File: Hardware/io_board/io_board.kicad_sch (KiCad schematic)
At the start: 32 parts, among them J1 Conn_01x40, J2 Conn_02x06_Odd_Even, J3 Mini-DIN-6, J4 Conn_02x10_Odd_Even, J5 Conn_01x04_Male, U2 W65C22NxP, U3 74LS14, U4 74HC137

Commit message: update for kicad 6
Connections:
- net GND: now also J4.13 (Pin_13)
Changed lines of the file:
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@@
   (junction (at 181.61 138.43) (diameter 0) (color 0 0 0 0)
   )
+  (junction (at 82.55 85.09) (diameter 0) (color 0 0 0 0)
+  )
   (junction (at 240.03 119.38) (diameter 0) (color 0 0 0 0)
   )
+  (junction (at 48.26 83.82) (diameter 0) (color 0 0 0 0)
+  )
   (junction (at 163.83 22.86) (diameter 0) (color 0 0 0 0)
   )
@@
     (stroke (width 0) (type default) (color 0 0 0 0))
   )
+  (wire (pts (xy 161.29 146.05) (xy 168.91 146.05))
+    (stroke (width 0) (type default) (color 0 0 0 0))
+  )
   (wire (pts (xy 181.61 153.67) (xy 186.69 153.67))
     (stroke (width 0) (type default) (color 0 0 0 0))
@@
     (stroke (width 0) (type default) (color 0 0 0 0))
   )
-  (wire (pts (xy 71.12 85.09) (xy 85.09 85.09))
+  (wire (pts (xy 71.12 85.09) (xy 82.55 85.09))
     (stroke (width 0) (type default) (color 0 0 0 0))
   )
@@
     (stroke (width 0) (type default) (color 0 0 0 0))
   )
+  (wire (pts (xy 48.26 83.82) (xy 46.99 83.82))
+    (stroke (width 0) (type default) (color 0 0 0 0))
+  )
   (wire (pts (xy 180.34 90.17) (xy 180.34 88.9))
     (stroke (width 0) (type default) (color 0 0 0 0))
@@
     (stroke (width 0) (type default) (color 0 0 0 0))
   )
-  (wire (pts (xy 53.34 83.82) (xy 46.99 83.82))
+  (wire (pts (xy 53.34 83.82) (xy 48.26 83.82))
     (stroke (width 0) (type default) (color 0 0 0 0))
   )
@@
   )
   (wire (pts (xy 101.6 83.82) (xy 96.52 83.82))
+    (stroke (width 0) (type default) (color 0 0 0 0))
+  )
+  (wire (pts (xy 82.55 85.09) (xy 85.09 85.09))
     (stroke (width 0) (type default) (color 0 0 0 0))
   )
@@
     (pin "1")
     (pin "2")
+    (pin "3")
+    (pin "4")
+    (pin "5")
+    (pin "6")
+    (pin "8")
+    (pin "9")
+    (pin "10")
+    (pin "11")
+    (pin "12")
+    (pin "13")
+    (pin "14")
+    (pin "7")
   )
   (symbol (lib_id "74xx:74LS14") (at 189.23 99.06 180) (unit 2)
@@
       (effects (font (size 1.27 1.27)) hide)
     )
+    (pin "1")
+    (pin "2")
     (pin "3")
     (pin "4")
+    (pin "5")
+    (pin "6")
+    (pin "8")
+    (pin "9")
+    (pin "10")
+    (pin "11")
+    (pin "12")
+    (pin "13")
+    (pin "14")
+    (pin "7")
   )
   (symbol (lib_id "74xx:74LS14") (at 48.26 161.29 0) (unit 3)
@@
       (effects (font (size 1.27 1.27)) hide)
     )
+    (pin "1")
+    (pin "2")
+    (pin "3")
+    (pin "4")
     (pin "5")
     (pin "6")
+    (pin "8")
+    (pin "9")
+    (pin "10")
+    (pin "11")
+    (pin "12")
+    (pin "13")
+    (pin "14")
+    (pin "7")
   )
   (symbol (lib_id "74xx:74LS14") (at 48.26 172.72 0) (unit 4)
@@
       (effects (font (size 1.27 1.27)) hide)
     )
+    (pin "1")
+    (pin "2")
+    (pin "3")
+    (pin "4")
+    (pin "5")
+    (pin "6")
     (pin "8")
     (pin "9")
+    (pin "10")
+    (pin "11")
+    (pin "12")
+    (pin "13")
+    (pin "14")
+    (pin "7")
   )
   (symbol (lib_id "74xx:74LS14") (at 196.85 86.36 180) (unit 5)
@@
       (effects (font (size 1.27 1.27)) hide)
     )
+    (pin "1")
+    (pin "2")
+    (pin "3")
+    (pin "4")
+    (pin "5")
+    (pin "6")
+    (pin "8")
+    (pin "9")
     (pin "10")
     (pin "11")
+    (pin "12")
+    (pin "13")
+    (pin "14")
+    (pin "7")
   )
   (symbol (lib_id "74xx:74LS14") (at 213.36 88.9 180) (unit 6)
@@
       (effects (font (size 1.27 1.27)) hide)
     )
+    (pin "1")
+    (pin "2")
+    (pin "3")
+    (pin "4")
+    (pin "5")
+    (pin "6")
+    (pin "8")
+    (pin "9")
+    (pin "10")
+    (pin "11")
     (pin "12")
     (pin "13")
+    (pin "14")
+    (pin "7")
   )
   (symbol (lib_id "74xx:74LS14") (at 240.03 140.97 0) (unit 7)
@@
       (effects (font (size 1.27 1.27)) hide)
     )
+    (pin "1")
+    (pin "2")
+    (pin "3")
+    (pin "4")
+    (pin "5")
+    (pin "6")
+    (pin "8")
+    (pin "9")
+    (pin "10")
+    (pin "11")
+    (pin "12")
+    (pin "13")
     (pin "14")
     (pin "7")
@@
     (pin "1")
   )
+  (symbol (lib_id "power:GND") (at 161.29 146.05 0) (unit 1)
+    (in_bom yes) (on_board yes)
+    (property "Reference" "#PWR0139" (id 0) (at 161.29 152.4 0)
+      (effects (font (size 1.27 1.27)) hide)
+    )
+    (property "Value" "GND" (id 1) (at 161.417 150.4442 0))
+    (property "Footprint" "" (id 2) (at 161.29 146.05 0)
+      (effects (font (size 1.27 1.27)) hide)
+    )
+    (property "Datasheet" "" (id 3) (at 161.29 146.05 0)
+      (effects (font (size 1.27 1.27)) hide)
+    )
+    (pin "1")
+  )
   (symbol (lib_id "74xx:74HC137") (at 119.38 142.24 0) (unit 1)
     (in_bom yes) (on_board yes) (fields_autoplaced)
@@
     (pin "9")
   )
+  (symbol (lib_id "power:PWR_FLAG") (at 48.26 83.82 0) (unit 1)
+    (in_bom yes) (on_board yes) (fields_autoplaced)
+    (property "Reference" "#FLG0101" (id 0) (at 48.26 81.915 0)
+      (effects (font (size 1.27 1.27)) hide)
+    )
+    (property "Value" "PWR_FLAG" (id 1) (at 48.26 80.2442 0))
+    (property "Footprint" "" (id 2) (at 48.26 83.82 0)
+      (effects (font (size 1.27 1.27)) hide)
+    )
+    (property "Datasheet" "~" (id 3) (at 48.26 83.82 0)
+      (effects (font (size 1.27 1.27)) hide)
+    )
+    (pin "1")
+  )
+  (symbol (lib_id "power:PWR_FLAG") (at 82.55 85.09 0) (unit 1)
+    (in_bom yes) (on_board yes) (fields_autoplaced)
+    (property "Reference" "#FLG0102" (id 0) (at 82.55 83.185 0)
+      (effects (font (size 1.27 1.27)) hide)
+    )
+    (property "Value" "PWR_FLAG" (id 1) (at 82.55 81.5142 0))
+    (property "Footprint" "" (id 2) (at 82.55 85.09 0)
+      (effects (font (size 1.27 1.27)) hide)
+    )
+    (property "Datasheet" "~" (id 3) (at 82.55 85.09 0)
+      (effects (font (size 1.27 1.27)) hide)
+    )
+    (pin "1")
+  )
   (sheet_instances
     (path "/" (page "1"))
   )
   (symbol_instances
+    (path "/af339d33-3531-42fd-aaba-73cbd73b724b"
+      (reference "#FLG0101") (unit 1) (value "PWR_FLAG") (footprint "")
+    )
+    (path "/e0ece25e-4db1-472a-896f-76e59008368f"
+      (reference "#FLG0102") (unit 1) (value "PWR_FLAG") (footprint "")
+    )
     (path "/00000000-0000-0000-0000-00005fd64472"
       (reference "#PWR0101") (unit 1) (value "+5V") (footprint "")
@@
       (reference "#PWR0138") (unit 1) (value "+5V") (footprint "")
     )
+    (path "/7512532e-08f1-4a9c-83bd-4429d275ecbb"
+      (reference "#PWR0139") (unit 1) (value "GND") (footprint "")
+    )
     (path "/00000000-0000-0000-0000-00005febb5d8"

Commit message: update io board
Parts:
- D1, D2, D3, D4, D5, D6, D7, D8: footprint LED_THT:LED_D3.0mm_Horizontal_O3.81mm_Z6.0mm -> w_conn_av:LED_D3.0mm_Horizontal_O3.81mm_Z6.0mm_2
- J3: footprint mini-din:MINI-DIN-6-FULL-SHIELD -> Custom_Footprints:Connector_Mini-DIN_Female_6Pin_2rows
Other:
- company: (none) -> Six Pixels
- title: (none) -> IO Board
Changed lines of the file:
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@@
 (kicad_sch (version 20211123) (generator eeschema)
   (paper "A4")
+  (title_block
+    (title "IO Board")
+    (date "2023-02-11")
+    (rev "${VERSION}")
+    (company "Six Pixels")
+    (comment 1 "Added pin header for PS/2")
+  )
   (junction (at 203.2 118.11) (diameter 0) (color 0 0 0 0)
   )
@@
     (property "Reference" "J3" (id 0) (at 215.9 108.7882 0))
     (property "Value" "Mini-DIN-6" (id 1) (at 217.17 110.49 0))
-    (property "Footprint" "mini-din:MINI-DIN-6-FULL-SHIELD" (id 2) (at 215.9 118.11 0)
+    (property "Footprint" "Custom_Footprints:Connector_Mini-DIN_Female_6Pin_2rows" (id 2) (at 215.9 118.11 0)
       (effects (font (size 1.27 1.27)) hide)
     )
@@
     (property "Reference" "D1" (id 0) (at 105.5878 40.2082 0))
     (property "Value" "LED" (id 1) (at 105.5878 42.5196 0))
-    (property "Footprint" "LED_THT:LED_D3.0mm_Horizontal_O3.81mm_Z6.0mm" (id 2) (at 105.41 45.72 0)
+    (property "Footprint" "w_conn_av:LED_D3.0mm_Horizontal_O3.81mm_Z6.0mm_2" (id 2) (at 105.41 45.72 0)
       (effects (font (size 1.27 1.27)) hide)
     )
@@
     (property "Reference" "D2" (id 0) (at 105.5878 46.5582 0))
     (property "Value" "LED" (id 1) (at 105.5878 48.8696 0))
-    (property "Footprint" "LED_THT:LED_D3.0mm_Horizontal_O3.81mm_Z6.0mm" (id 2) (at 105.41 52.07 0)
+    (property "Footprint" "w_conn_av:LED_D3.0mm_Horizontal_O3.81mm_Z6.0mm_2" (id 2) (at 105.41 52.07 0)
       (effects (font (size 1.27 1.27)) hide)
     )
@@
     (property "Reference" "D3" (id 0) (at 105.5878 52.9082 0))
     (property "Value" "LED" (id 1) (at 105.5878 55.2196 0))
-    (property "Footprint" "LED_THT:LED_D3.0mm_Horizontal_O3.81mm_Z6.0mm" (id 2) (at 105.41 58.42 0)
+    (property "Footprint" "w_conn_av:LED_D3.0mm_Horizontal_O3.81mm_Z6.0mm_2" (id 2) (at 105.41 58.42 0)
       (effects (font (size 1.27 1.27)) hide)
     )
@@
     (property "Reference" "D4" (id 0) (at 105.5878 59.2582 0))
     (property "Value" "LED" (id 1) (at 105.5878 61.5696 0))
-    (property "Footprint" "LED_THT:LED_D3.0mm_Horizontal_O3.81mm_Z6.0mm" (id 2) (at 105.41 64.77 0)
+    (property "Footprint" "w_conn_av:LED_D3.0mm_Horizontal_O3.81mm_Z6.0mm_2" (id 2) (at 105.41 64.77 0)
       (effects (font (size 1.27 1.27)) hide)
     )
@@
     (property "Reference" "D5" (id 0) (at 105.5878 65.6082 0))
     (property "Value" "LED" (id 1) (at 105.5878 67.9196 0))
-    (property "Footprint" "LED_THT:LED_D3.0mm_Horizontal_O3.81mm_Z6.0mm" (id 2) (at 105.41 71.12 0)
+    (property "Footprint" "w_conn_av:LED_D3.0mm_Horizontal_O3.81mm_Z6.0mm_2" (id 2) (at 105.41 71.12 0)
       (effects (font (size 1.27 1.27)) hide)
     )
@@
     (property "Reference" "D6" (id 0) (at 105.5878 71.9582 0))
     (property "Value" "LED" (id 1) (at 105.5878 74.2696 0))
-    (property "Footprint" "LED_THT:LED_D3.0mm_Horizontal_O3.81mm_Z6.0mm" (id 2) (at 105.41 77.47 0)
+    (property "Footprint" "w_conn_av:LED_D3.0mm_Horizontal_O3.81mm_Z6.0mm_2" (id 2) (at 105.41 77.47 0)
       (effects (font (size 1.27 1.27)) hide)
     )
@@
     (property "Reference" "D7" (id 0) (at 105.5878 78.3082 0))
     (property "Value" "LED" (id 1) (at 105.5878 80.6196 0))
-    (property "Footprint" "LED_THT:LED_D3.0mm_Horizontal_O3.81mm_Z6.0mm" (id 2) (at 105.41 83.82 0)
+    (property "Footprint" "w_conn_av:LED_D3.0mm_Horizontal_O3.81mm_Z6.0mm_2" (id 2) (at 105.41 83.82 0)
       (effects (font (size 1.27 1.27)) hide)
     )
@@
     (property "Reference" "D8" (id 0) (at 105.5878 84.6582 0))
     (property "Value" "LED" (id 1) (at 105.5878 86.9696 0))
-    (property "Footprint" "LED_THT:LED_D3.0mm_Horizontal_O3.81mm_Z6.0mm" (id 2) (at 105.41 90.17 0)
+    (property "Footprint" "w_conn_av:LED_D3.0mm_Horizontal_O3.81mm_Z6.0mm_2" (id 2) (at 105.41 90.17 0)
       (effects (font (size 1.27 1.27)) hide)
     )
@@
     )
     (path "/00000000-0000-0000-0000-00005ff231e9"
-      (reference "D1") (unit 1) (value "LED") (footprint "LED_THT:LED_D3.0mm_Horizontal_O3.81mm_Z6.0mm")
+      (reference "D1") (unit 1) (value "LED") (footprint "w_conn_av:LED_D3.0mm_Horizontal_O3.81mm_Z6.0mm_2")
     )
     (path "/00000000-0000-0000-0000-00005ff4ddfd"
-      (reference "D2") (unit 1) (value "LED") (footprint "LED_THT:LED_D3.0mm_Horizontal_O3.81mm_Z6.0mm")
+      (reference "D2") (unit 1) (value "LED") (footprint "w_conn_av:LED_D3.0mm_Horizontal_O3.81mm_Z6.0mm_2")
     )
     (path "/00000000-0000-0000-0000-00005ff55550"
-      (reference "D3") (unit 1) (value "LED") (footprint "LED_THT:LED_D3.0mm_Horizontal_O3.81mm_Z6.0mm")
+      (reference "D3") (unit 1) (value "LED") (footprint "w_conn_av:LED_D3.0mm_Horizontal_O3.81mm_Z6.0mm_2")
     )
     (path "/00000000-0000-0000-0000-00005ff5cdd6"
-      (reference "D4") (unit 1) (value "LED") (footprint "LED_THT:LED_D3.0mm_Horizontal_O3.81mm_Z6.0mm")
+      (reference "D4") (unit 1) (value "LED") (footprint "w_conn_av:LED_D3.0mm_Horizontal_O3.81mm_Z6.0mm_2")
     )
     (path "/00000000-0000-0000-0000-00005ff64552"
-      (reference "D5") (unit 1) (value "LED") (footprint "LED_THT:LED_D3.0mm_Horizontal_O3.81mm_Z6.0mm")
+      (reference "D5") (unit 1) (value "LED") (footprint "w_conn_av:LED_D3.0mm_Horizontal_O3.81mm_Z6.0mm_2")
     )
     (path "/00000000-0000-0000-0000-00005ff6c107"
-      (reference "D6") (unit 1) (value "LED") (footprint "LED_THT:LED_D3.0mm_Horizontal_O3.81mm_Z6.0mm")
+      (reference "D6") (unit 1) (value "LED") (footprint "w_conn_av:LED_D3.0mm_Horizontal_O3.81mm_Z6.0mm_2")
     )
     (path "/00000000-0000-0000-0000-00005ff73ab8"
-      (reference "D7") (unit 1) (value "LED") (footprint "LED_THT:LED_D3.0mm_Horizontal_O3.81mm_Z6.0mm")
+      (reference "D7") (unit 1) (value "LED") (footprint "w_conn_av:LED_D3.0mm_Horizontal_O3.81mm_Z6.0mm_2")
     )
     (path "/00000000-0000-0000-0000-00005ff7b8a8"
-      (reference "D8") (unit 1) (value "LED") (footprint "LED_THT:LED_D3.0mm_Horizontal_O3.81mm_Z6.0mm")
+      (reference "D8") (unit 1) (value "LED") (footprint "w_conn_av:LED_D3.0mm_Horizontal_O3.81mm_Z6.0mm_2")
     )
     (path "/00000000-0000-0000-0000-00005fd62dcd"
@@
     )
     (path "/00000000-0000-0000-0000-00005fd93536"
-      (reference "J3") (unit 1) (value "Mini-DIN-6") (footprint "mini-din:MINI-DIN-6-FULL-SHIELD")
+      (reference "J3") (unit 1) (value "Mini-DIN-6") (footprint "Custom_Footprints:Connector_Mini-DIN_Female_6Pin_2rows")
     )
     (path "/00000000-0000-0000-0000-00005ff16c05"

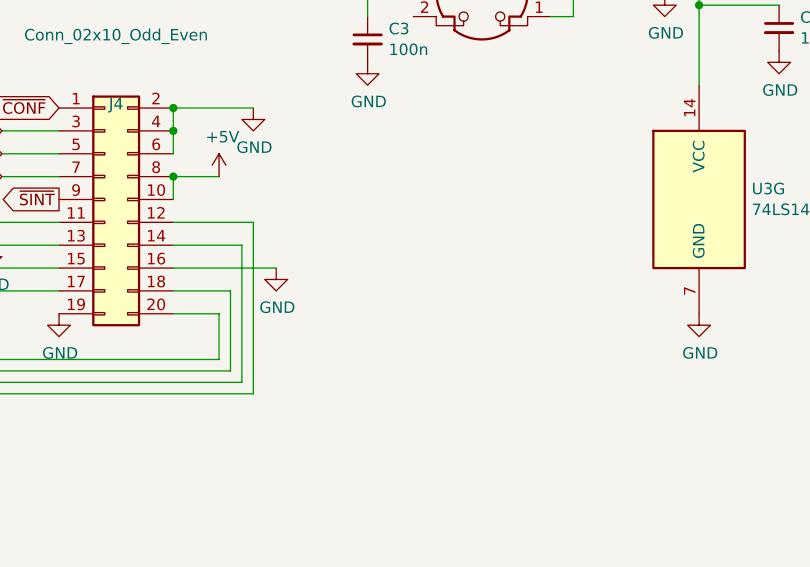
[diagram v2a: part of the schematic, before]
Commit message: Can read file and list directories
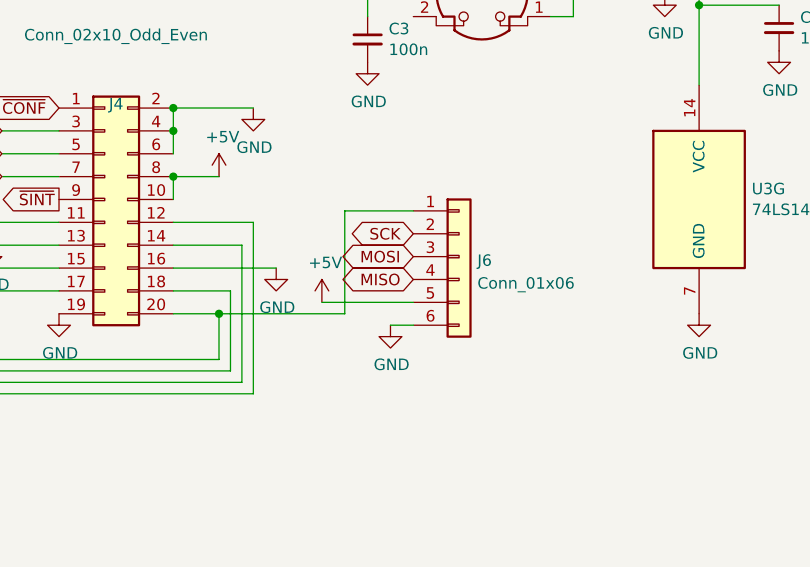
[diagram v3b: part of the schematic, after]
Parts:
- added J6: Conn_01x06, Connector_PinSocket_2.54mm:PinSocket_1x06_P2.54mm_Vertical, symbol Connector_Generic:Conn_01x06
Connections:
- net +5V: now also J6.5 (Pin_5)
- net GND: now also J6.6 (Pin_6)
- net LED4: now also J6.2 (Pin_2)
- net MISO: now also J6.4 (Pin_4)
- net MOSI: now also J6.3 (Pin_3)
- net SS1: now also J6.1 (Pin_1)
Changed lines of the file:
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@@
   (junction (at 223.52 111.76) (diameter 0) (color 0 0 0 0)
   )
+  (junction (at 186.69 153.67) (diameter 0) (color 0 0 0 0)
+  )
   (junction (at 181.61 130.81) (diameter 0) (color 0 0 0 0)
   )
@@
     (stroke (width 0) (type default) (color 0 0 0 0))
   )
+  (wire (pts (xy 200.66 153.67) (xy 186.69 153.67))
+    (stroke (width 0) (type default) (color 0 0 0 0))
+  )
   (wire (pts (xy 194.31 45.72) (xy 204.47 45.72))
     (stroke (width 0) (type default) (color 0 0 0 0))
@@
     (stroke (width 0) (type default) (color 0 0 0 0))
   )
+  (wire (pts (xy 200.66 142.24) (xy 200.66 153.67))
+    (stroke (width 0) (type default) (color 0 0 0 0))
+  )
   (wire (pts (xy 106.68 137.16) (xy 109.22 137.16))
     (stroke (width 0) (type default) (color 0 0 0 0))
@@
     (stroke (width 0) (type default) (color 0 0 0 0))
   )
+  (wire (pts (xy 208.28 142.24) (xy 200.66 142.24))
+    (stroke (width 0) (type default) (color 0 0 0 0))
+  )
   (wire (pts (xy 190.5 58.42) (xy 179.07 58.42))
     (stroke (width 0) (type default) (color 0 0 0 0))
@@
     (stroke (width 0) (type default) (color 0 0 0 0))
   )
+  (wire (pts (xy 205.74 154.94) (xy 208.28 154.94))
+    (stroke (width 0) (type default) (color 0 0 0 0))
+  )
   (wire (pts (xy 101.6 45.72) (xy 96.52 45.72))
     (stroke (width 0) (type default) (color 0 0 0 0))
@@
   )
   (wire (pts (xy 181.61 130.81) (xy 190.5 130.81))
+    (stroke (width 0) (type default) (color 0 0 0 0))
+  )
+  (wire (pts (xy 198.12 152.4) (xy 208.28 152.4))
     (stroke (width 0) (type default) (color 0 0 0 0))
   )
@@
     )
   )
+  (global_label "MISO" (shape bidirectional) (at 208.28 149.86 180) (fields_autoplaced)
+    (effects (font (size 1.27 1.27)) (justify right))
+    (property "Intersheet References" "${INTERSHEET_REFS}" (id 0) (at 45.72 11.43 0)
+      (effects (font (size 1.27 1.27)) hide)
+    )
+  )
   (global_label "~{CONF}" (shape bidirectional) (at 107.95 142.24 180) (fields_autoplaced)
     (effects (font (size 1.27 1.27)) (justify right))
@@
     (effects (font (size 1.27 1.27)) (justify left))
     (property "Intersheet References" "${INTERSHEET_REFS}" (id 0) (at 0 0 0)
+      (effects (font (size 1.27 1.27)) hide)
+    )
+  )
+  (global_label "SCK" (shape bidirectional) (at 208.28 144.78 180) (fields_autoplaced)
+    (effects (font (size 1.27 1.27)) (justify right))
+    (property "Intersheet References" "${INTERSHEET_REFS}" (id 0) (at 45.72 11.43 0)
       (effects (font (size 1.27 1.27)) hide)
     )
@@
     (effects (font (size 1.27 1.27)) (justify left))
     (property "Intersheet References" "${INTERSHEET_REFS}" (id 0) (at 0 0 0)
+      (effects (font (size 1.27 1.27)) hide)
+    )
+  )
+  (global_label "MOSI" (shape bidirectional) (at 208.28 147.32 180) (fields_autoplaced)
+    (effects (font (size 1.27 1.27)) (justify right))
+    (property "Intersheet References" "${INTERSHEET_REFS}" (id 0) (at 45.72 11.43 0)
       (effects (font (size 1.27 1.27)) hide)
     )
@@
     (pin "9")
   )
+  (symbol (lib_id "power:+5V") (at 198.12 152.4 0) (unit 1)
+    (in_bom yes) (on_board yes)
+    (property "Reference" "#PWR0141" (id 0) (at 198.12 156.21 0)
+      (effects (font (size 1.27 1.27)) hide)
+    )
+    (property "Value" "+5V" (id 1) (at 198.501 148.0058 0))
+    (property "Footprint" "" (id 2) (at 198.12 152.4 0)
+      (effects (font (size 1.27 1.27)) hide)
+    )
+    (property "Datasheet" "" (id 3) (at 198.12 152.4 0)
+      (effects (font (size 1.27 1.27)) hide)
+    )
+    (pin "1")
+  )
   (symbol (lib_id "power:GND") (at 251.46 83.82 0) (unit 1)
     (in_bom yes) (on_board yes)
@@
     (pin "1")
   )
+  (symbol (lib_id "power:GND") (at 205.74 154.94 0) (unit 1)
+    (in_bom yes) (on_board yes)
+    (property "Reference" "#PWR0140" (id 0) (at 205.74 161.29 0)
+      (effects (font (size 1.27 1.27)) hide)
+    )
+    (property "Value" "GND" (id 1) (at 205.867 159.3342 0))
+    (property "Footprint" "" (id 2) (at 205.74 154.94 0)
+      (effects (font (size 1.27 1.27)) hide)
+    )
+    (property "Datasheet" "" (id 3) (at 205.74 154.94 0)
+      (effects (font (size 1.27 1.27)) hide)
+    )
+    (pin "1")
+  )
   (symbol (lib_id "power:PWR_FLAG") (at 82.55 85.09 0) (unit 1)
     (in_bom yes) (on_board yes) (fields_autoplaced)
@@
     (pin "1")
   )
+  (symbol (lib_id "Connector_Generic:Conn_01x06") (at 213.36 147.32 0) (unit 1)
+    (in_bom yes) (on_board yes) (fields_autoplaced)
+    (property "Reference" "J6" (id 0) (at 215.392 147.7553 0)
+      (effects (font (size 1.27 1.27)) (justify left))
+    )
+    (property "Value" "Conn_01x06" (id 1) (at 215.392 150.2922 0)
+      (effects (font (size 1.27 1.27)) (justify left))
+    )
+    (property "Footprint" "Connector_PinSocket_2.54mm:PinSocket_1x06_P2.54mm_Vertical" (id 2) (at 213.36 147.32 0)
+      (effects (font (size 1.27 1.27)) hide)
+    )
+    (property "Datasheet" "~" (id 3) (at 213.36 147.32 0)
+      (effects (font (size 1.27 1.27)) hide)
+    )
+    (pin "1")
+    (pin "2")
+    (pin "3")
+    (pin "4")
+    (pin "5")
+    (pin "6")
+  )
   (sheet_instances
     (path "/" (page "1"))
@@
       (reference "#PWR0139") (unit 1) (value "GND") (footprint "")
     )
+    (path "/c6a74144-0fd5-47d0-8896-5cf6857ec3a9"
+      (reference "#PWR0140") (unit 1) (value "GND") (footprint "")
+    )
+    (path "/00d722eb-830c-4436-be2b-eb690e4fb3d0"
+      (reference "#PWR0141") (unit 1) (value "+5V") (footprint "")
+    )
     (path "/00000000-0000-0000-0000-00005febb5d8"
       (reference "C1") (unit 1) (value "10n") (footprint "Capacitor_THT:C_Disc_D4.7mm_W2.5mm_P5.00mm")
@@
       (reference "J5") (unit 1) (value "Conn_01x04_Male") (footprint "Connector_PinHeader_2.54mm:PinHeader_1x04_P2.54mm_Vertical")
     )
+    (path "/ed886d48-6d9a-48d0-a504-a33d38fedb6b"
+      (reference "J6") (unit 1) (value "Conn_01x06") (footprint "Connector_PinSocket_2.54mm:PinSocket_1x06_P2.54mm_Vertical")
+    )
     (path "/00000000-0000-0000-0000-00005ff71274"
